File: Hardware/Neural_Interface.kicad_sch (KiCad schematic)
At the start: 8 parts, among them SW1 RESET, SW2 BOOT

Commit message: Power Management Complete
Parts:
- added R10, R11, R9: 4.7k, Resistor_SMD:R_0402_1005Metric, symbol Device:R
- added U3: TMP117, Package_BGA:Texas_DSBGA-6_0.95x1.488mm_Layout2x3_P0.4mm, symbol Motor_Driver:TMP117
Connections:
- net +3.3V: now also R10.2, R11.2, R9.2, U3.B1 (V+)
- net GND: now also U3.B2 (GND), U3.C1 (ADD0)
- new net ALERT: R11.1, U3.C2 (ALERT)
- new net SCL: R9.1, U3.A2 (SCL)
- new net SDA: R10.1, U3.A1 (SDA)
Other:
- note added: "Micro-Controller"
- note added: "Temperature Sensor"
- moved on the sheet: C1, C2, C3, C4, R1, SW1, SW2, U1

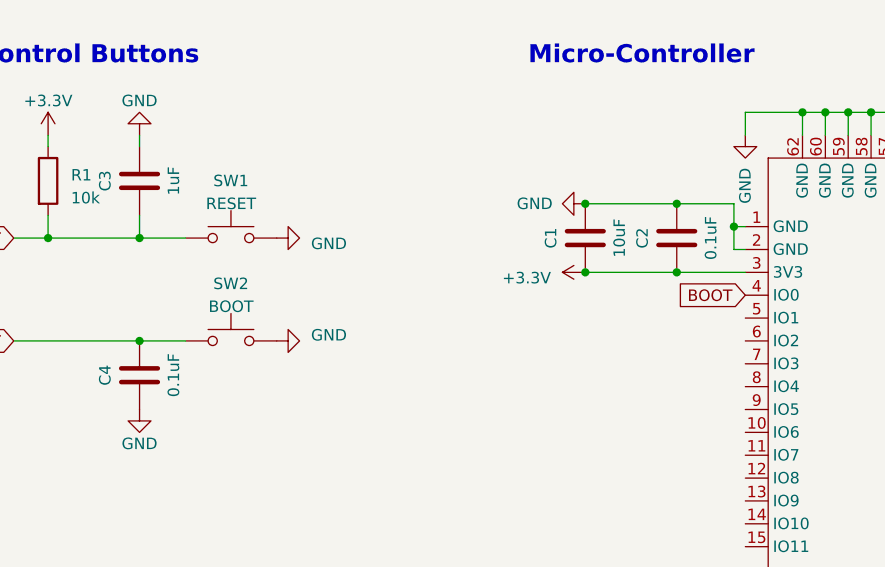
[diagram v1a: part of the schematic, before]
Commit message: Design Analog Frontend
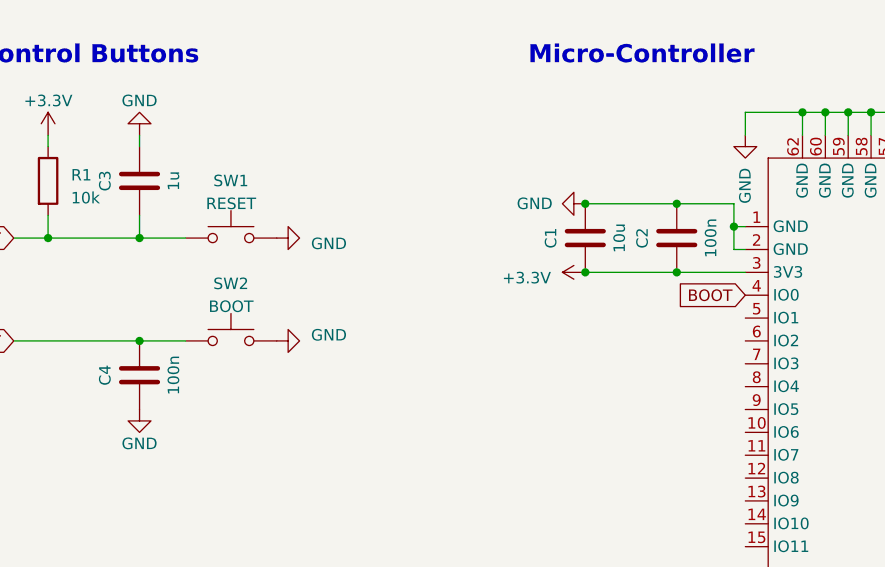
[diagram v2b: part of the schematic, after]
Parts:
- C1: value 10uF -> 10u; footprint Capacitor_SMD:C_1210_3225Metric -> (none)
- C2, C4: value 0.1uF -> 100n; footprint Capacitor_SMD:C_0603_1608Metric -> (none)
- C3: value 1uF -> 1u; footprint Capacitor_SMD:C_0805_2012Metric -> (none)
- R1: footprint Resistor_SMD:R_0805_2012Metric -> (none)
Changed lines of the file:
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@@
       (effects (font (size 1.27 1.27)))
     )
-    (property "Value" "0.1uF" (at 109.22 80.01 90)
-      (effects (font (size 1.27 1.27)))
-    )
-    (property "Footprint" "Capacitor_SMD:C_0603_1608Metric" (at 104.4448 76.2 0)
+    (property "Value" "100n" (at 109.22 80.01 90)
+      (effects (font (size 1.27 1.27)))
+    )
+    (property "Footprint" "" (at 104.4448 76.2 0)
       (effects (font (size 1.27 1.27)) hide)
     )
@@
       (effects (font (size 1.27 1.27)) (justify left))
     )
-    (property "Footprint" "Resistor_SMD:R_0805_2012Metric" (at 33.782 73.66 90)
+    (property "Footprint" "" (at 33.782 73.66 90)
       (effects (font (size 1.27 1.27)) hide)
     )
@@
       (effects (font (size 1.27 1.27)))
     )
-    (property "Value" "10uF" (at 99.06 80.01 90)
-      (effects (font (size 1.27 1.27)))
-    )
-    (property "Footprint" "Capacitor_SMD:C_1210_3225Metric" (at 94.2848 76.2 0)
+    (property "Value" "10u" (at 99.06 80.01 90)
+      (effects (font (size 1.27 1.27)))
+    )
+    (property "Footprint" "" (at 94.2848 76.2 0)
       (effects (font (size 1.27 1.27)) hide)
     )
@@
       (effects (font (size 1.27 1.27)))
     )
-    (property "Value" "0.1uF" (at 49.53 95.25 90)
-      (effects (font (size 1.27 1.27)))
-    )
-    (property "Footprint" "Capacitor_SMD:C_0603_1608Metric" (at 44.7548 91.44 0)
+    (property "Value" "100n" (at 49.53 95.25 90)
+      (effects (font (size 1.27 1.27)))
+    )
+    (property "Footprint" "" (at 44.7548 91.44 0)
       (effects (font (size 1.27 1.27)) hide)
     )
@@
       (effects (font (size 1.27 1.27)))
     )
-    (property "Value" "1uF" (at 49.53 73.66 90)
-      (effects (font (size 1.27 1.27)))
-    )
-    (property "Footprint" "Capacitor_SMD:C_0805_2012Metric" (at 44.7548 69.85 0)
-      (effects (font (size 1.27 1.27)) hide)
-    )
+    (property "Value" "1u" (at 49.53 73.66 90)
+      (effects (font (size 1.27 1.27)))
+    )
+    (property "Footprint" "" (at 44.7548 69.85 0)
+      (effects (font (size 1.27 1.27)) hide)
+    )

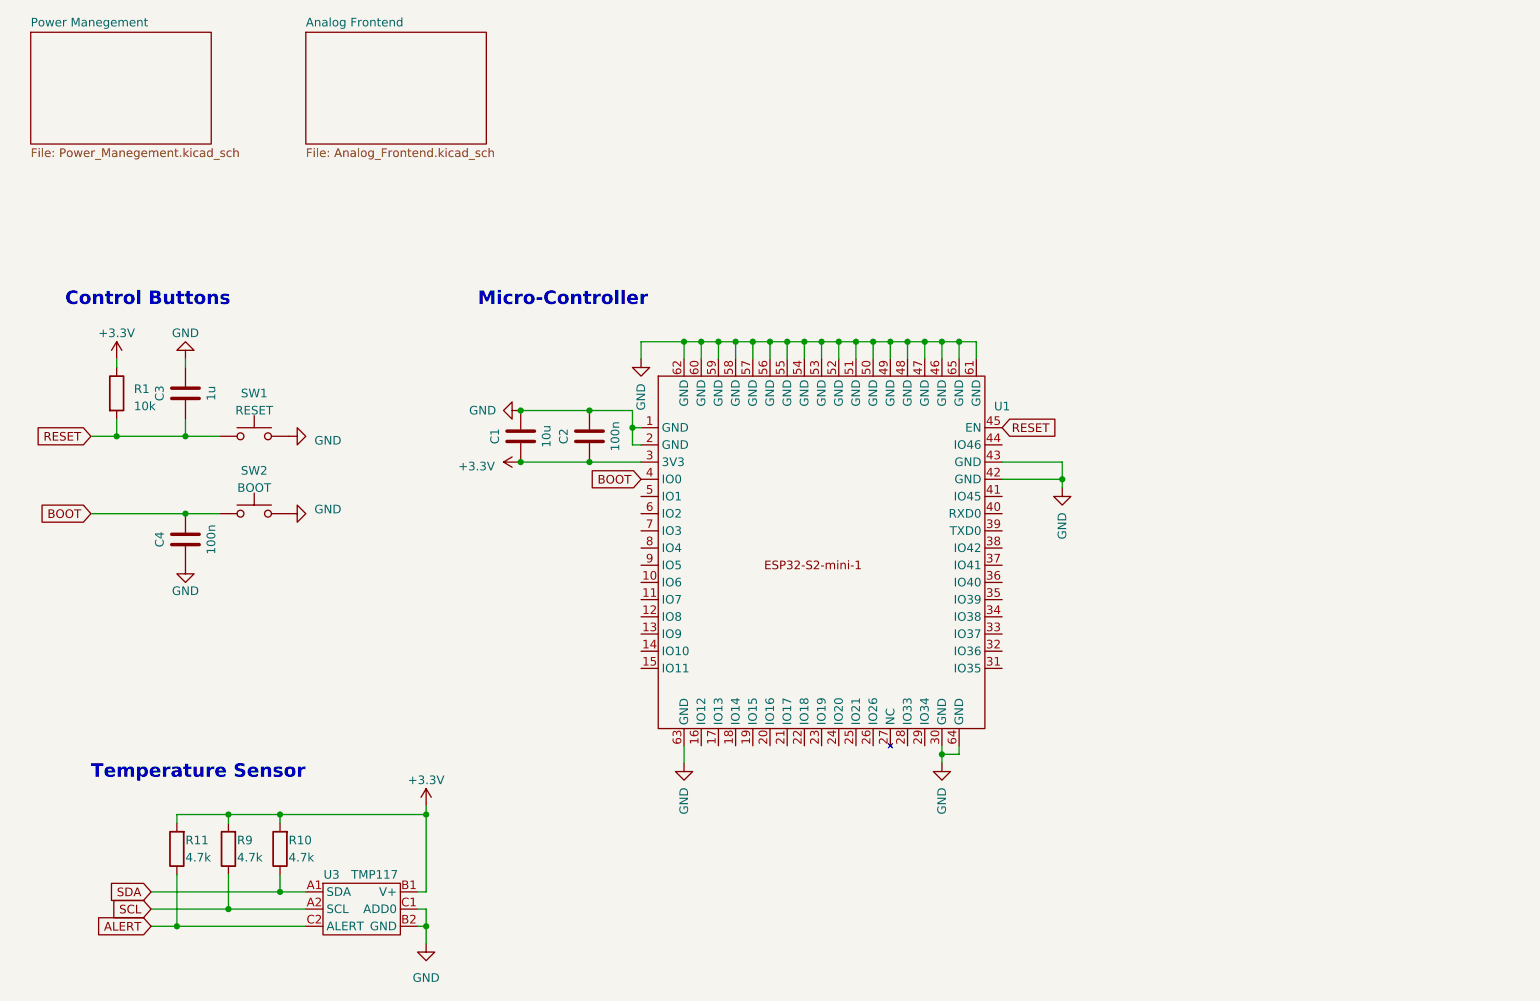
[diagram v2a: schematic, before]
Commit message: Spec all components
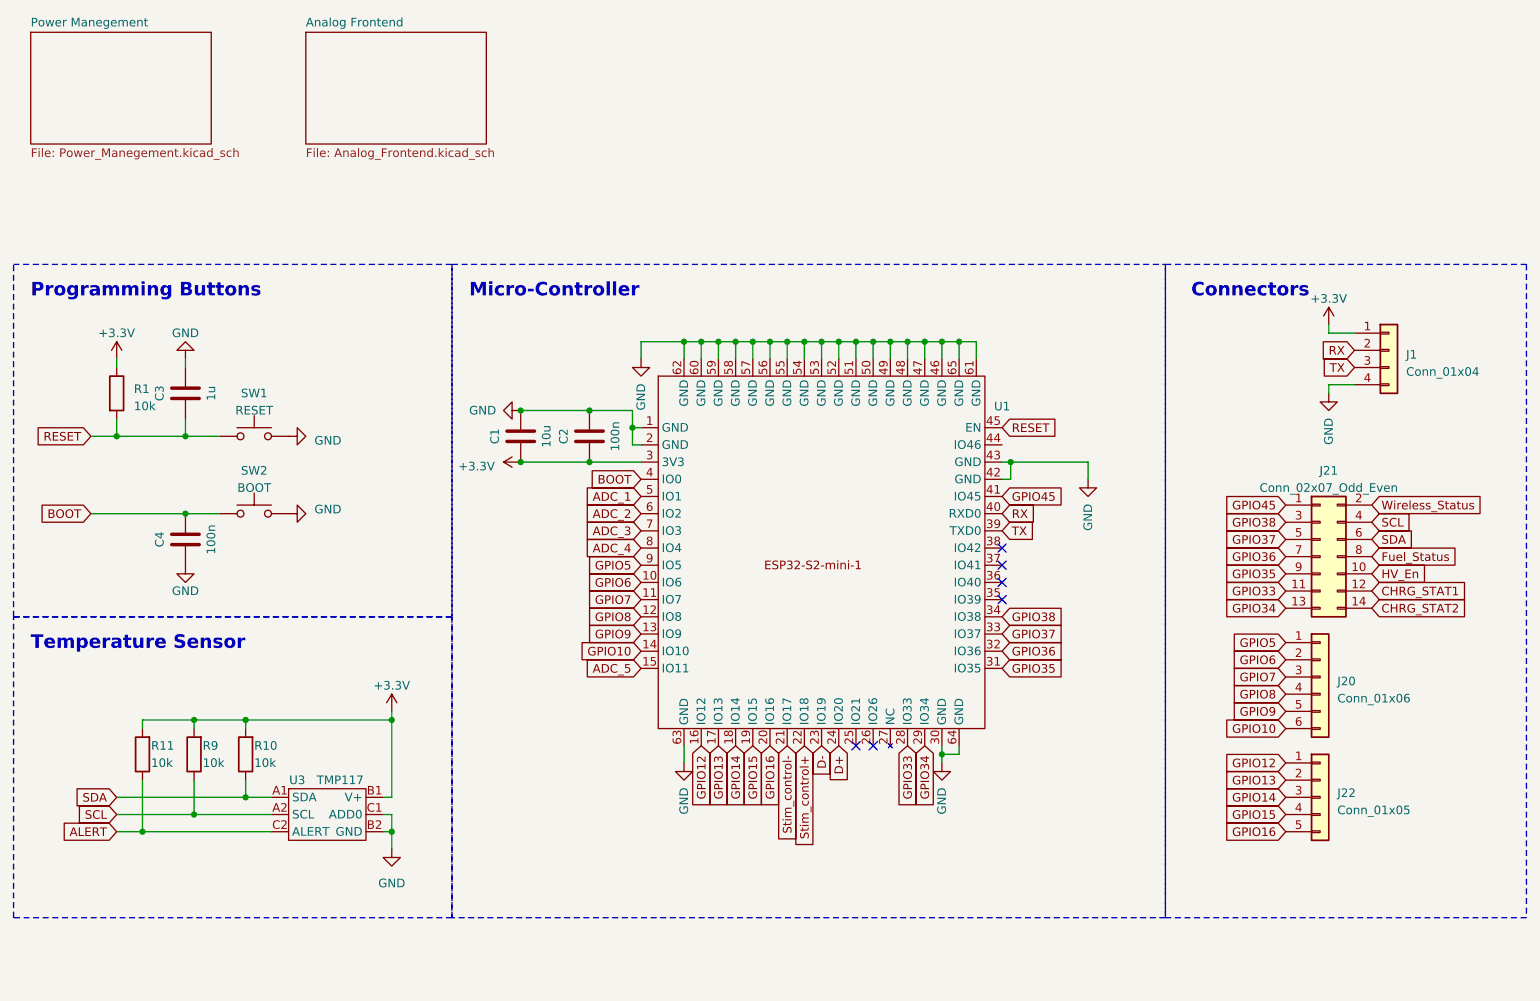
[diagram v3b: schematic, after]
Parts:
- added J1: Conn_01x04, Connector_PinHeader_2.54mm:PinHeader_1x04_P2.54mm_Vertical, symbol Connector_Generic:Conn_01x04
- added J20: Conn_01x06, Connector_PinHeader_2.54mm:PinHeader_1x06_P2.54mm_Vertical, symbol Connector_Generic:Conn_01x06
- added J21: Conn_02x07_Odd_Even, Connector_PinHeader_2.54mm:PinHeader_2x07_P2.54mm_Vertical, symbol Connector_Generic:Conn_02x07_Odd_Even
- added J22: Conn_01x05, Connector_PinHeader_2.54mm:PinHeader_1x05_P2.54mm_Vertical, symbol Connector_Generic:Conn_01x05
- C1: footprint (none) -> Capacitor_SMD:C_0805_2012Metric
- C2, C4: footprint (none) -> Capacitor_SMD:C_0402_1005Metric
- C3: footprint (none) -> Capacitor_SMD:C_0603_1608Metric
- R1: footprint (none) -> Resistor_SMD:R_0402_1005Metric
- R10, R11, R9: value 4.7k -> 10k
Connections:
- net +3.3V: now also J1.1 (Pin_1)
- net GND: now also J1.4 (Pin_4)
- net SCL: now also J21.4 (Pin_4)
- net SDA: now also J21.6 (Pin_6)
- net GPIO6: now reaches U1.10 (IO6)
- net GPIO6: now also J20.2 (Pin_2)
- net GPIO7: now reaches U1.11 (IO7)
- net GPIO7: now also J20.3 (Pin_3)
- net GPIO8: now reaches U1.12 (IO8)
- net GPIO8: now also J20.4 (Pin_4)
- net GPIO9: now reaches U1.13 (IO9)
- net GPIO9: now also J20.5 (Pin_5)
- net GPIO10: now reaches U1.14 (IO10)
- net GPIO10: now also J20.6 (Pin_6)
- net ADC_5: now reaches U1.15 (IO11)
- net GPIO12: now reaches U1.16 (IO12)
- net GPIO12: now also J22.1 (Pin_1)
- net GPIO13: now reaches U1.17 (IO13)
- net GPIO13: now also J22.2 (Pin_2)
- net GPIO14: now reaches U1.18 (IO14)
- net GPIO14: now also J22.3 (Pin_3)
- net GPIO15: now reaches U1.19 (IO15)
- net GPIO15: now also J22.4 (Pin_4)
- net GPIO16: now reaches U1.20 (IO16)
- net GPIO16: now also J22.5 (Pin_5)
- net Stim_control-: now reaches U1.21 (IO17)
- net Stim_control+: now reaches U1.22 (IO18)
- net D-: now reaches U1.23 (IO19)
- net D+: now reaches U1.24 (IO20)
- net GPIO33: now reaches U1.28 (IO33)
- net GPIO33: now also J21.11 (Pin_11)
- net GPIO34: now reaches U1.29 (IO34)
- net GPIO34: now also J21.13 (Pin_13)
- net GPIO35: now reaches U1.31 (IO35)
- net GPIO35: now also J21.9 (Pin_9)
- net GPIO36: now reaches U1.32 (IO36)
- net GPIO36: now also J21.7 (Pin_7)
- net GPIO37: now reaches U1.33 (IO37)
- net GPIO37: now also J21.5 (Pin_5)
- net GPIO38: now reaches U1.34 (IO38)
- net GPIO38: now also J21.3 (Pin_3)
- net TX: now reaches U1.39 (TXD0)
- net TX: now also J1.3 (Pin_3)
- net RX: now reaches U1.40 (RXD0)
- net RX: now also J1.2 (Pin_2)
- net GPIO45: now reaches U1.41 (IO45)
- net GPIO45: now also J21.1 (Pin_1)
- net ADC_1: now reaches U1.5 (IO1)
- net ADC_2: now reaches U1.6 (IO2)
- net ADC_3: now reaches U1.7 (IO3)
- net ADC_4: now reaches U1.8 (IO4)
- net GPIO5: now reaches U1.9 (IO5)
- net GPIO5: now also J20.1 (Pin_1)
- new net CHRG_STAT1: J21.12 (Pin_12)
- new net CHRG_STAT2: J21.14 (Pin_14)
- new net Fuel_Status: J21.8 (Pin_8)
- new net HV_En: J21.10 (Pin_10)
- new net Wireless_Status: J21.2 (Pin_2)
- no-connect marks 0 -> 6
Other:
- note added: "Connectors"
- note added: "Programming Buttons"
- note removed: "Control Buttons"
- moved on the sheet: R10, R11, R9, U3

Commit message: Start Layout
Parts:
- removed J20: Conn_01x06, Connector_PinHeader_2.54mm:PinHeader_1x06_P2.54mm_Vertical, symbol Connector_Generic:Conn_01x06
- added J2: Conn_02x06_Odd_Even, Connector_PinSocket_2.54mm:PinSocket_2x06_P2.54mm_Vertical, symbol Connector_Generic:Conn_02x06_Odd_Even
- renumbered J21 to J1, J22 to J3, J1 to J4
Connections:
- net GPIO10: now also J2.11 (Pin_11)
- net GPIO33: now also J1.13 (Pin_13); no longer J1.11 (Pin_11)
- net GPIO34: now also J1.11 (Pin_11); no longer J1.13 (Pin_13)
- net GPIO5: now also J2.1 (Pin_1)
- net GPIO6: now also J2.3 (Pin_3)
- net GPIO7: now also J2.5 (Pin_5)
- net GPIO8: now also J2.7 (Pin_7)
- net GPIO9: now also J2.9 (Pin_9)
- new net MCLK: J2.2 (Pin_2)
- new net SCK: J2.10 (Pin_10)
- new net SDI: J2.8 (Pin_8)
- new net SDO: J2.6 (Pin_6)
- new net ~{CS}: J2.12 (Pin_12)
- new net ~{IRQ}: J2.4 (Pin_4)
